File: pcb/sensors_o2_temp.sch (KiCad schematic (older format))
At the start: 20 parts

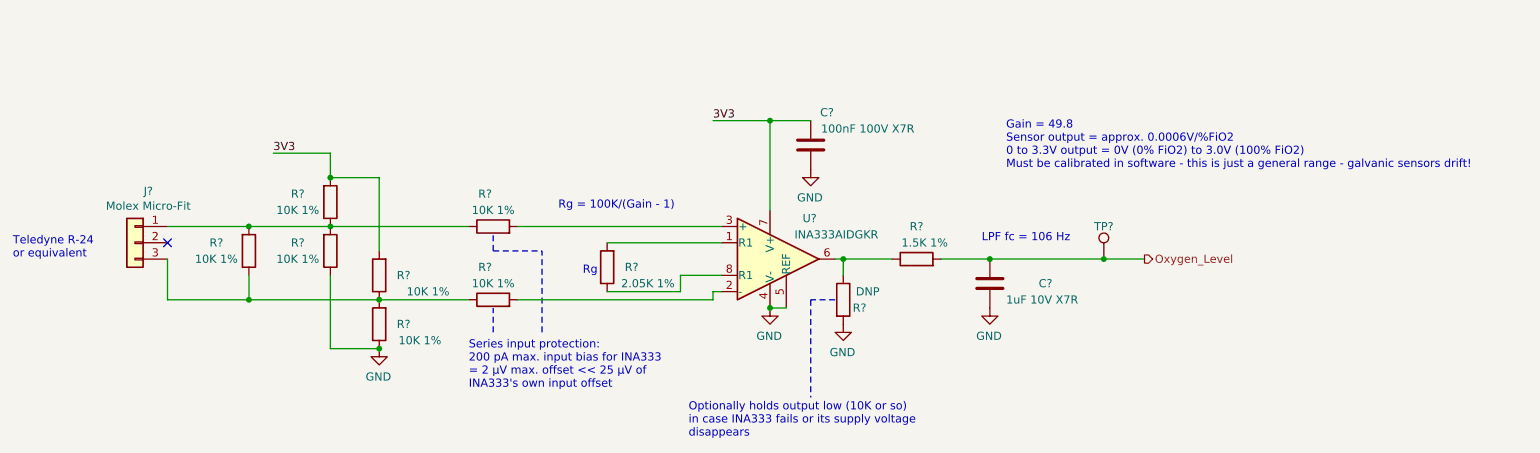
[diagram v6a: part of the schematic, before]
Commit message: CC-I2C, BOM
Added missing pull-ups on CC-SDA, CC-SCL
First pass at BOM consolidation
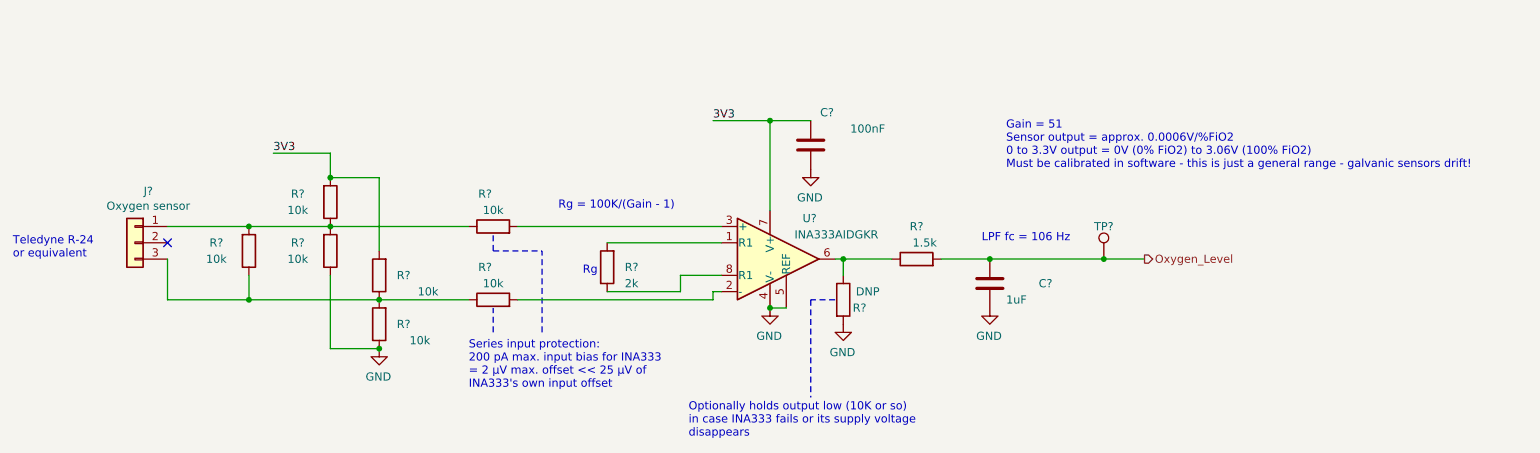
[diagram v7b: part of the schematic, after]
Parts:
- C?: value 100nF 100V X7R -> 100nF
- C?: value 1uF 10V X7R -> 1uF; Manufacturer (none) -> AVX; Part Number (none) -> 06035C104JAT2A
- J?: value Molex Micro-Fit -> Oxygen sensor
- R?: value 2.05K 1% -> 2k; Manufacturer KOA Speer -> (none)
- R? (x7): value 10K 1% -> 10k
- R?: value 1.5K 1% -> 1.5k
- R?: DNP (none) -> DNP
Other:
- note added: "Gain = 51\nSensor output = approx. 0.0006V/%FiO2\n0 to 3.3V output = 0V (0% FiO2) to 3.06V (100% FiO2)\nMust be calibrated in software - this is just a general range - galvanic sensors drift!"
- note removed: "Gain = 49.8\nSensor output = approx. 0.0006V/%FiO2\n0 to 3.3V output = 0V (0% FiO2) to 3.0V (100% FiO2)\nMust be calibrated in software - this is just a general range - galvanic sensors drift!"
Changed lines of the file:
@@
 AR Path="/5FCD4EEA/60132AA8" Ref="R?"  Part="1"
 F 0 "R?" H 4250 6000 50  0000 C CNN
-F 1 "2.05K 1%" H 4150 6100 50  0000 C CNN
+F 1 "2k" H 4250 6100 50  0000 C CNN
 F 2 "RespiraWorks_Std:R_0603_1608Metric" V 4330 6000 50  0001 C CNN
 F 3 "~" H 4400 6000 50  0001 C CNN
-F 4 "KOA Speer" H 4400 6000 50  0001 C CNN "Manufacturer"
+F 4 "" H 4400 6000 50  0001 C CNN "Manufacturer"
 F 5 "RK73H2BTTD1004F" H 4400 6000 50  0001 C CNN "Part Number"
 	1    4400 6000
@@
 AR Path="/5FCD4EEA/60132AB6" Ref="C?"  Part="1"
 F 0 "C?" H 5750 5050 50  0000 C CNN
-F 1 "100nF 100V X7R" H 6000 5150 50  0000 C CNN
+F 1 "100nF" H 6000 5150 50  0000 C CNN
 F 2 "RespiraWorks_Std:C_0603_1608Metric" H 5688 5100 50  0001 C CNN
 F 3 "~" H 5650 5250 50  0001 C CNN
@@
 	5100 5850 4400 5850
 Text Notes 6850 5400 0    50   ~ 0
-Gain = 49.8\nSensor output = approx. 0.0006V/%FiO2\n0 to 3.3V output = 0V (0% FiO2) to 3.0V (100% FiO2)\nMust be calibrated in software - this is just a general range - galvanic sensors drift!
+Gain = 51\nSensor output = approx. 0.0006V/%FiO2\n0 to 3.3V output = 0V (0% FiO2) to 3.06V (100% FiO2)\nMust be calibrated in software - this is just a general range - galvanic sensors drift!
 $Comp
 L Device:R R?
@@
 AR Path="/5FCD4EEA/60132ACE" Ref="R?"  Part="1"
 F 0 "R?" H 2850 6050 50  0000 C CNN
-F 1 "10K 1%" H 2700 6150 50  0000 C CNN
+F 1 "10k" H 2700 6150 50  0000 C CNN
 F 2 "RespiraWorks_Std:R_0603_1608Metric" V 2930 6050 50  0001 C CNN
 F 3 "~" H 3000 6050 50  0001 C CNN
@@
 AR Path="/5FCD4EEA/60132AD6" Ref="R?"  Part="1"
 F 0 "R?" H 2850 6350 50  0000 C CNN
-F 1 "10K 1%" H 2750 6450 50  0000 C CNN
+F 1 "10k" H 2750 6450 50  0000 C CNN
 F 2 "RespiraWorks_Std:R_0603_1608Metric" V 2930 6350 50  0001 C CNN
 F 3 "~" H 3000 6350 50  0001 C CNN
@@
 AR Path="/5FCD4EEA/60132AF8" Ref="J?"  Part="1"
 F 0 "J?" H 1418 6167 50  0000 C CNN
-F 1 "Molex Micro-Fit" H 1418 6076 50  0000 C CNN
+F 1 "Oxygen sensor" H 1418 6076 50  0000 C CNN
 F 2 "RespiraWorks_Std:Molex_Micro-Fit_3.0_43650-0315_1x03_P3.00mm_Vertical" H 1500 5850 50  0001 C CNN
 F 3 "~" H 1500 5850 50  0001 C CNN
@@
 AR Path="/5FCD4EEA/60132B07" Ref="R?"  Part="1"
 F 0 "R?" V 6500 5950 50  0000 C CNN
-F 1 "1.5K 1%" V 6400 5900 50  0000 C CNN
+F 1 "1.5k" V 6400 5900 50  0000 C CNN
 F 2 "RespiraWorks_Std:R_0603_1608Metric" V 6230 5950 50  0001 C CNN
 F 3 "~" H 6300 5950 50  0001 C CNN
@@
 AR Path="/5FCD4EEA/60132B0E" Ref="C?"  Part="1"
 F 0 "C?" H 7050 6100 50  0000 L CNN
-F 1 "1uF 10V X7R" H 6850 6200 50  0000 L CNN
+F 1 "1uF" H 6850 6200 50  0000 L CNN
 F 2 "RespiraWorks_Std:C_0603_1608Metric" H 6788 5950 50  0001 C CNN
 F 3 "~" H 6750 6100 50  0001 C CNN
+F 4 "AVX" H 6750 6100 50  0001 C CNN "Manufacturer"
+F 5 "06035C104JAT2A" H 6750 6100 50  0001 C CNN "Part Number"
 	1    6750 6100
 	1    0    0    1
@@
 F 4 "KOA Speer" H 5850 6200 50  0001 C CNN "Manufacturer"
 F 5 "RK73H2BTTD1004F" H 5850 6200 50  0001 C CNN "Part Number"
+F 6 "DNP" H 5850 6200 50  0001 C CNN "DNP"
 	1    5850 6200
 	1    0    0    -1
@@
 AR Path="/5FCD4EEA/60132B33" Ref="R?"  Part="1"
 F 0 "R?" V 3900 5800 50  0000 C CNN
-F 1 "10K 1%" V 3800 5750 50  0000 C CNN
+F 1 "10k" V 3800 5750 50  0000 C CNN
 F 2 "RespiraWorks_Std:R_0603_1608Metric" V 3630 5750 50  0001 C CNN
 F 3 "~" H 3700 5750 50  0001 C CNN
@@
 AR Path="/5FCD4EEA/601505E1" Ref="R?"  Part="1"
 F 0 "R?" V 3900 6250 50  0000 C CNN
-F 1 "10K 1%" V 3800 6200 50  0000 C CNN
+F 1 "10k" V 3800 6200 50  0000 C CNN
 F 2 "RespiraWorks_Std:R_0603_1608Metric" V 3630 6200 50  0001 C CNN
 F 3 "~" H 3700 6200 50  0001 C CNN
@@
 AR Path="/5FCD4EEA/60153672" Ref="R?"  Part="1"
 F 0 "R?" H 2500 5550 50  0000 C CNN
-F 1 "10K 1%" H 2500 5650 50  0000 C CNN
+F 1 "10k" H 2500 5650 50  0000 C CNN
 F 2 "RespiraWorks_Std:R_0603_1608Metric" V 2630 5600 50  0001 C CNN
 F 3 "~" H 2700 5600 50  0001 C CNN
@@
 AR Path="/5FCD4EEA/601544DC" Ref="R?"  Part="1"
 F 0 "R?" H 2000 5850 50  0000 C CNN
-F 1 "10K 1%" H 2000 5950 50  0000 C CNN
+F 1 "10k" H 2000 5950 50  0000 C CNN
 F 2 "RespiraWorks_Std:R_0603_1608Metric" V 2130 5900 50  0001 C CNN
 F 3 "~" H 2200 5900 50  0001 C CNN
@@
 AR Path="/5FCD4EEA/6015D0A5" Ref="R?"  Part="1"
 F 0 "R?" H 2500 5850 50  0000 C CNN
-F 1 "10K 1%" H 2500 5950 50  0000 C CNN
+F 1 "10k" H 2500 5950 50  0000 C CNN
 F 2 "RespiraWorks_Std:R_0603_1608Metric" V 2630 5900 50  0001 C CNN
 F 3 "~" H 2700 5900 50  0001 C CNN
@@
 AR Path="/5FCD4D18/60F7C3BE" Ref="TP?"  Part="1"
 AR Path="/5FCD4B8E/60F7C3BE" Ref="TP?"  Part="1"
+AR Path="/5FCD4EEA/60F7C3BE" Ref="TP?"  Part="1"
 F 0 "TP?" H 7450 6150 50  0000 C CNN
 F 1 "TP" V 7500 6000 50  0001 C CNN

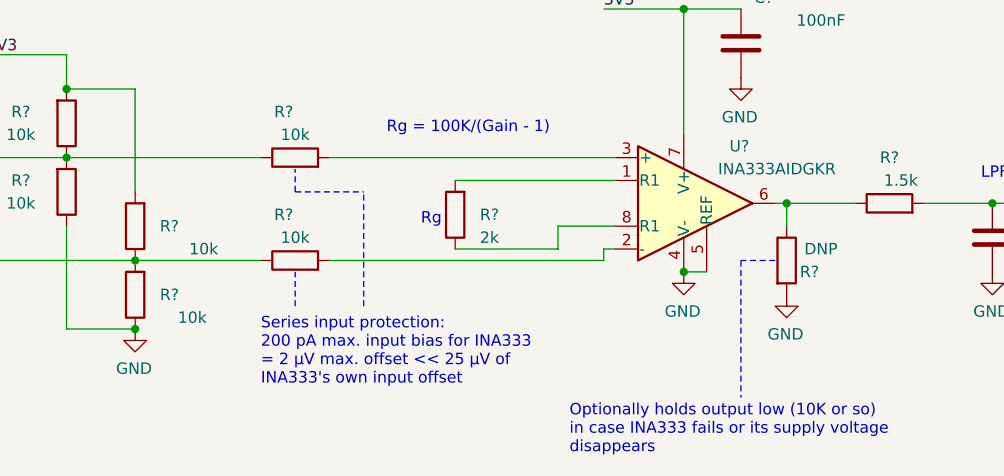
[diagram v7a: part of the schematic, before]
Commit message: BOM
More BOM consolidation with bulk capacitors + changed tantalum stepper caps to aluminum, added bulk cap to PSol driver
Made stepper's 3.3V power naming consistent with others (3.3V->3V3)
Slightly increased current limit on PSOL/heater driver
Changed 3906 transistors to 2907 to better support +5V_Batt current
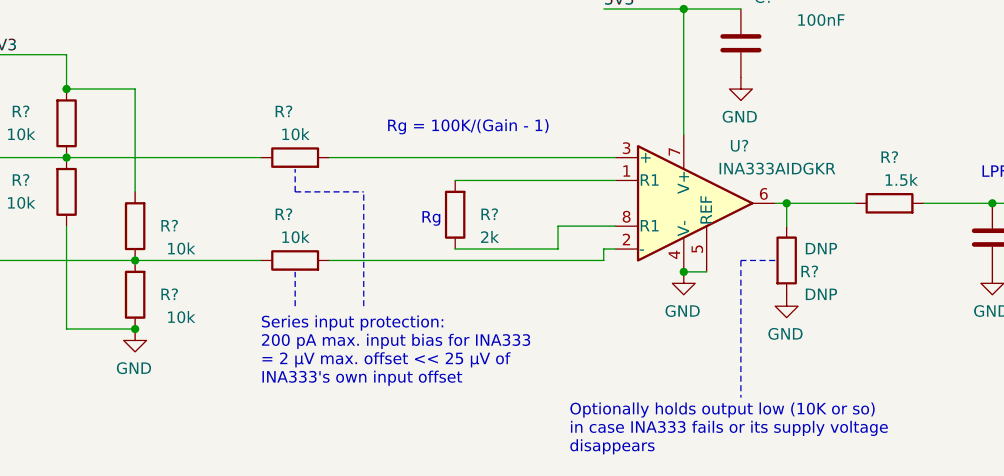
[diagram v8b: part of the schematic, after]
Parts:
- C?: Part Number 06035C104JAT2A -> (none)
- R? (x10): Part Number RK73H2BTTD1004F -> (none)
- TP?: footprint (none) -> RespiraWorks_Std:TestPoint_Pad_2.0x2.0mm
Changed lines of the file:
@@
 F 3 "~" H 4400 6000 50  0001 C CNN
 F 4 "" H 4400 6000 50  0001 C CNN "Manufacturer"
-F 5 "RK73H2BTTD1004F" H 4400 6000 50  0001 C CNN "Part Number"
 	1    4400 6000
 	-1   0    0    1
@@
 F 3 "~" H 5650 5250 50  0001 C CNN
 F 4 "" H 5650 5250 50  0001 C CNN "Manufacturer"
-F 5 "" H 5650 5250 50  0001 C CNN "Part Number"
 	1    5650 5250
 	1    0    0    1
@@
 AR Path="/5FCD4EEA/60132ACE" Ref="R?"  Part="1"
 F 0 "R?" H 2850 6050 50  0000 C CNN
-F 1 "10k" H 2700 6150 50  0000 C CNN
+F 1 "10k" H 2800 6150 50  0000 C CNN
 F 2 "RespiraWorks_Std:R_0603_1608Metric" V 2930 6050 50  0001 C CNN
 F 3 "~" H 3000 6050 50  0001 C CNN
 F 4 "KOA Speer" H 3000 6050 50  0001 C CNN "Manufacturer"
-F 5 "RK73H2BTTD1004F" H 3000 6050 50  0001 C CNN "Part Number"
 	1    3000 6050
 	-1   0    0    1
@@
 AR Path="/5FCD4EEA/60132AD6" Ref="R?"  Part="1"
 F 0 "R?" H 2850 6350 50  0000 C CNN
-F 1 "10k" H 2750 6450 50  0000 C CNN
+F 1 "10k" H 2800 6450 50  0000 C CNN
 F 2 "RespiraWorks_Std:R_0603_1608Metric" V 2930 6350 50  0001 C CNN
 F 3 "~" H 3000 6350 50  0001 C CNN
 F 4 "KOA Speer" H 3000 6350 50  0001 C CNN "Manufacturer"
-F 5 "RK73H2BTTD1004F" H 3000 6350 50  0001 C CNN "Part Number"
 	1    3000 6350
 	-1   0    0    1
@@
 F 3 "~" H 6300 5950 50  0001 C CNN
 F 4 "KOA Speer" H 6300 5950 50  0001 C CNN "Manufacturer"
-F 5 "RK73H2BTTD1004F" H 6300 5950 50  0001 C CNN "Part Number"
 	1    6300 5950
 	0    -1   -1   0
@@
 F 3 "~" H 6750 6100 50  0001 C CNN
 F 4 "AVX" H 6750 6100 50  0001 C CNN "Manufacturer"
-F 5 "06035C104JAT2A" H 6750 6100 50  0001 C CNN "Part Number"
 	1    6750 6100
 	1    0    0    1
@@
 F 3 "~" H 5850 6200 50  0001 C CNN
 F 4 "KOA Speer" H 5850 6200 50  0001 C CNN "Manufacturer"
-F 5 "RK73H2BTTD1004F" H 5850 6200 50  0001 C CNN "Part Number"
-F 6 "DNP" H 5850 6200 50  0001 C CNN "DNP"
+F 5 "DNP" H 6000 6050 50  0000 C CNN "DNP"
 	1    5850 6200
 	1    0    0    -1
@@
 F 3 "~" H 3700 5750 50  0001 C CNN
 F 4 "KOA Speer" H 3700 5750 50  0001 C CNN "Manufacturer"
-F 5 "RK73H2BTTD1004F" H 3700 5750 50  0001 C CNN "Part Number"
 	1    3700 5750
 	0    -1   -1   0
@@
 F 3 "~" H 3700 6200 50  0001 C CNN
 F 4 "KOA Speer" H 3700 6200 50  0001 C CNN "Manufacturer"
-F 5 "RK73H2BTTD1004F" H 3700 6200 50  0001 C CNN "Part Number"
 	1    3700 6200
 	0    -1   -1   0
@@
 F 3 "~" H 2700 5600 50  0001 C CNN
 F 4 "KOA Speer" H 2700 5600 50  0001 C CNN "Manufacturer"
-F 5 "RK73H2BTTD1004F" H 2700 5600 50  0001 C CNN "Part Number"
 	1    2700 5600
 	1    0    0    1
@@
 F 3 "~" H 2200 5900 50  0001 C CNN
 F 4 "KOA Speer" H 2200 5900 50  0001 C CNN "Manufacturer"
-F 5 "RK73H2BTTD1004F" H 2200 5900 50  0001 C CNN "Part Number"
 	1    2200 5900
 	1    0    0    1
@@
 F 3 "~" H 2700 5900 50  0001 C CNN
 F 4 "KOA Speer" H 2700 5900 50  0001 C CNN "Manufacturer"
-F 5 "RK73H2BTTD1004F" H 2700 5900 50  0001 C CNN "Part Number"
 	1    2700 5900
 	1    0    0    1
@@
 F 0 "TP?" H 7450 6150 50  0000 C CNN
 F 1 "TP" V 7500 6000 50  0001 C CNN
-F 2 "" H 7650 5950 50  0001 C CNN
+F 2 "RespiraWorks_Std:TestPoint_Pad_2.0x2.0mm" H 7650 5950 50  0001 C CNN
 F 3 "~" H 7650 5950 50  0001 C CNN
 	1    7450 5950
